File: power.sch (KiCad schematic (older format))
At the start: 52 parts, among them J2 USB_C_Receptacle_USB2.0, Q1 FS8205A, Q6 2N7002, Q7 AO3401A, Q8 2N7002, U3 SY7088, U4 XC6206P332MR, U5 DW01+G, U6 TP4056, U9 BQ34Z100

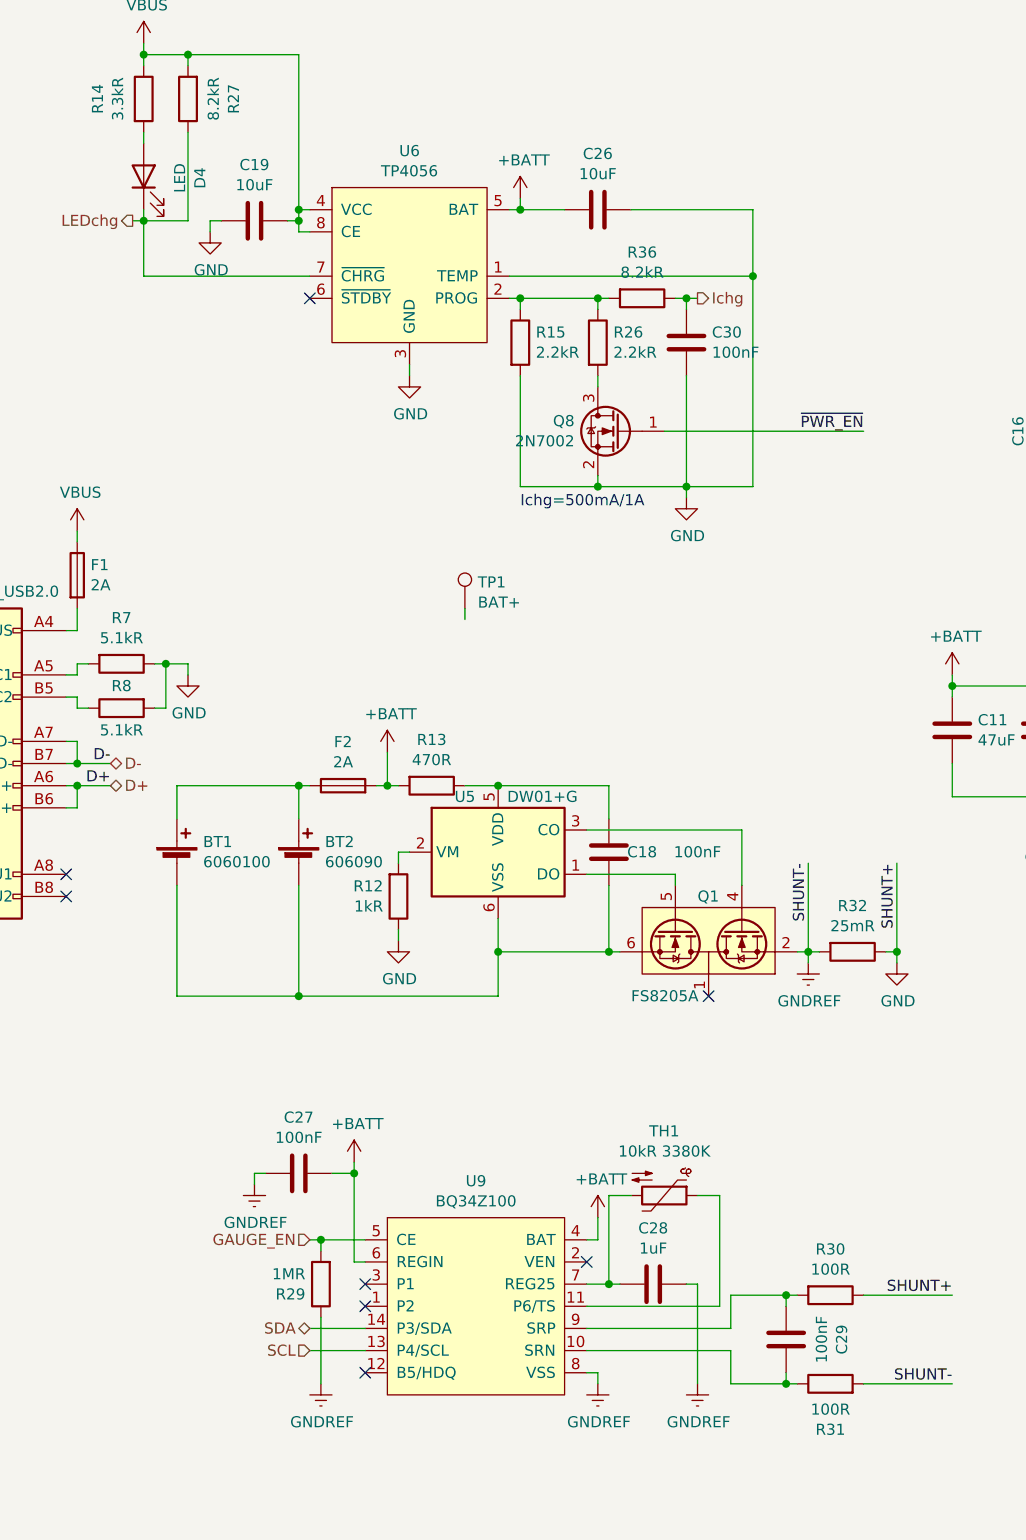
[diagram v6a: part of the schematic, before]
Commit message: Route SD interface
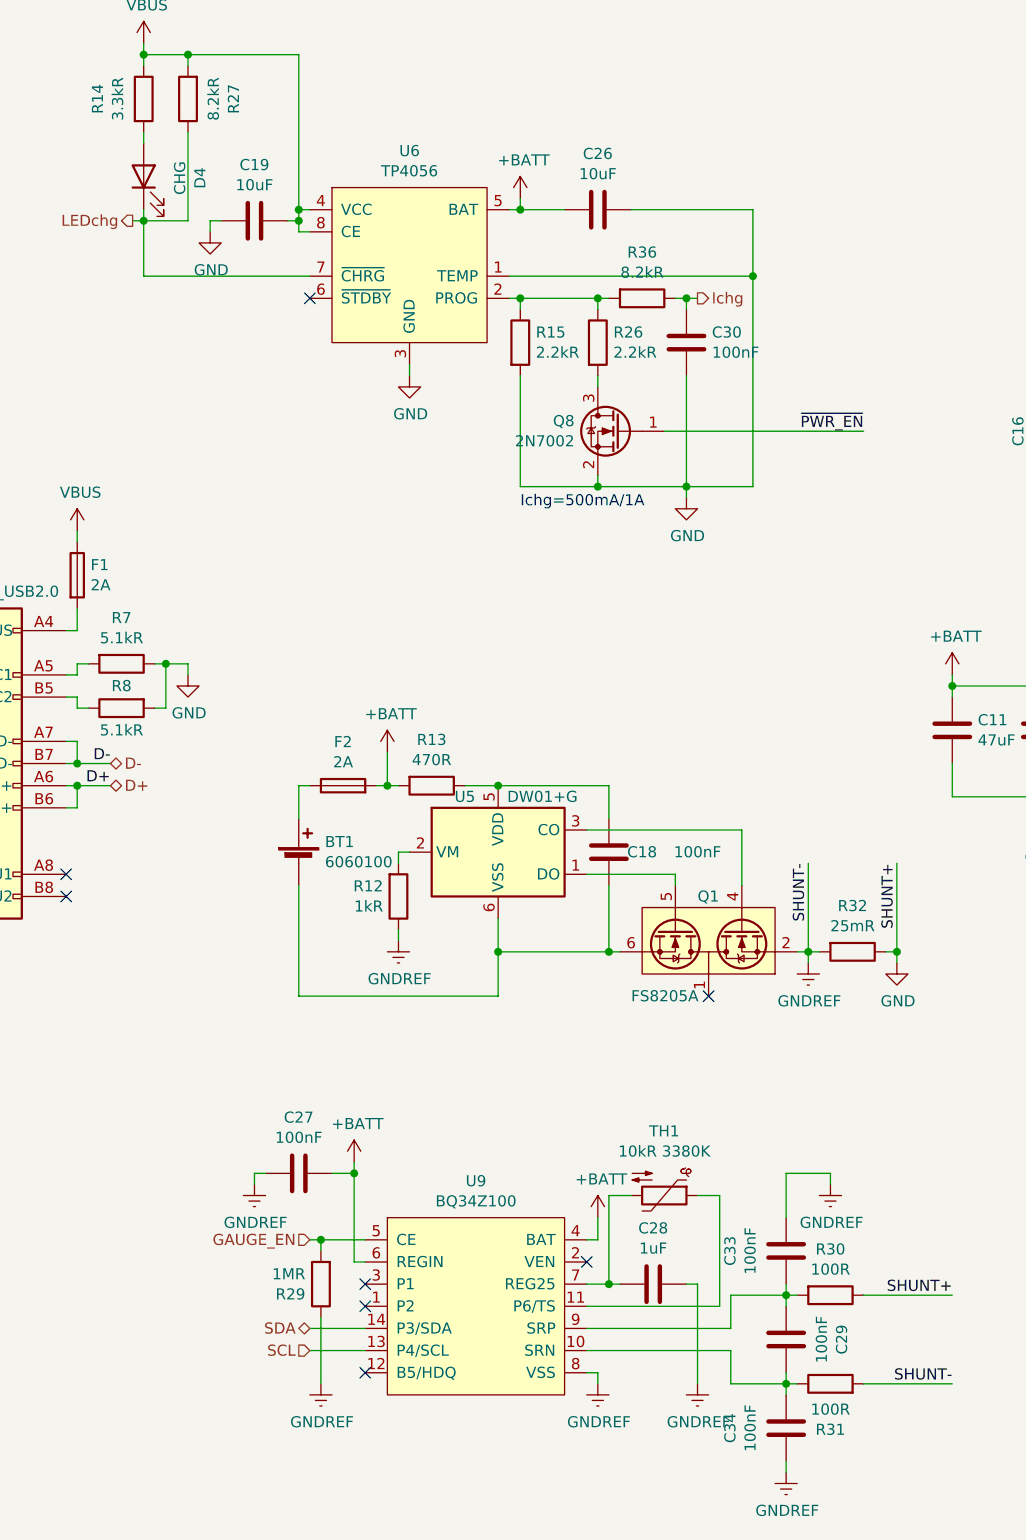
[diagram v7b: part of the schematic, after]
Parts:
- removed BT2: 606090, Battery_LiPo:LiPo_606090, symbol Device:Battery_Cell
- removed TP1: BAT+, TestPoint:TestPoint_Pad_4.0x4.0mm, symbol Connector:TestPoint
- added C33, C34: 100nF, Capacitor_SMD:C_0402_1005Metric, symbol Device:C
- D4: value LED -> CHG
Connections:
- net GND: no longer R12.1
- net GNDREF: now also R12.1, C33.2, C34.1
- net at C29.2, R31.1, U9.10 (SRN): now also C34.2
- net at C29.1, R30.2, U9.9 (SRP): now also C33.1
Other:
- moved on the sheet: BT1
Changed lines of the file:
@@
 	1    0    0    1
 $EndComp
-$Comp
-L power:GND #PWR?
-U 1 1 6057E172
-P 3150 4800
-AR Path="/6057E172" Ref="#PWR?"  Part="1"
-AR Path="/6051E9DC/6057E172" Ref="#PWR035"  Part="1"
-F 0 "#PWR035" H 3150 4550 50  0001 C CNN
-F 1 "GND" H 3155 4627 50  0000 C CNN
-F 2 "" H 3150 4800 50  0001 C CNN
-F 3 "" H 3150 4800 50  0001 C CNN
-	1    3150 4800
-	1    0    0    -1
-$EndComp
 Connection ~ 3600 4100
-$Comp
-L Connector:TestPoint TP?
-U 1 1 6057E186
-P 3450 3300
-AR Path="/6057E186" Ref="TP?"  Part="1"
-AR Path="/6051E9DC/6057E186" Ref="TP1"  Part="1"
-F 0 "TP1" H 3508 3418 50  0000 L CNN
-F 1 "BAT+" H 3508 3327 50  0000 L CNN
-F 2 "TestPoint:TestPoint_Pad_4.0x4.0mm" H 3650 3300 50  0001 C CNN
-F 3 "~" H 3650 3300 50  0001 C CNN
-	1    3450 3300
-	1    0    0    -1
-$EndComp
 $Comp
 L Transistor_FET_Dual:FS8205A Q?
@@
 AR Path="/6051E9DC/6057E1D2" Ref="D4"  Part="1"
 F 0 "D4" H 1993 1095 50  0000 C CNN
-F 1 "LED" H 1993 1186 50  0000 C CNN
+F 1 "CHG" H 1993 1186 50  0000 C CNN
 F 2 "LED_SMD:LED_0603_1608Metric" H 2000 1350 50  0001 C CNN
 F 3 "" H 2000 1350 50  0001 C CNN
@@
 	0    -1   -1   0
 $EndComp
-Wire Wire Line
-	3450 3350 3450 3300
 $Comp
 L Device:R R?
@@
 	3150 4450 3150 4400
 $Comp
-L Device:Battery_Cell BT2
-U 1 1 61944CD6
+L Device:Battery_Cell BT1
+U 1 1 6195E7B9
 P 2700 4450
-F 0 "BT2" H 2818 4546 50  0000 L CNN
-F 1 "606090" H 2818 4455 50  0000 L CNN
-F 2 "Battery_LiPo:LiPo_606090" V 2700 4510 50  0001 C CNN
+F 0 "BT1" H 2818 4546 50  0000 L CNN
+F 1 "6060100" H 2818 4455 50  0000 L CNN
+F 2 "Battery_LiPo:LiPo_6060100" V 2700 4510 50  0001 C CNN
 F 3 "~" V 2700 4510 50  0001 C CNN
 	1    2700 4450
 	1    0    0    -1
 $EndComp
-$Comp
-L Device:Battery_Cell BT1
-U 1 1 6195E7B9
-P 2150 4450
-F 0 "BT1" H 2268 4546 50  0000 L CNN
-F 1 "6060100" H 2268 4455 50  0000 L CNN
-F 2 "Battery_LiPo:LiPo_6060100" V 2150 4510 50  0001 C CNN
-F 3 "~" V 2150 4510 50  0001 C CNN
-	1    2150 4450
-	1    0    0    -1
-$EndComp
 Wire Wire Line
 	3050 4100 3100 4100
@@
 Connection ~ 3600 4850
 Wire Wire Line
-	2700 5050 2150 5050
-Wire Wire Line
-	2150 5050 2150 4550
-Connection ~ 2700 5050
-Wire Wire Line
-	2150 4100 2150 4250
-Wire Wire Line
 	2700 4250 2700 4100
 Wire Wire Line
-	2150 4100 2700 4100
-Connection ~ 2700 4100
-Wire Wire Line
 	2700 4100 2750 4100
+$Comp
+L Device:C C?
+U 1 1 61A24F0F
+P 4900 6200
+AR Path="/61A24F0F" Ref="C?"  Part="1"
+AR Path="/6051E9DC/61A24F0F" Ref="C33"  Part="1"
+F 0 "C33" V 5152 6200 50  0000 C CNN
+F 1 "100nF" V 5061 6200 50  0000 C CNN
+F 2 "Capacitor_SMD:C_0402_1005Metric" H 4938 6050 50  0001 C CNN
+F 3 "~" H 4900 6200 50  0001 C CNN
+F 4 "C1525" H 4900 6200 50  0001 C CNN "LCSC"
+	1    4900 6200
+	-1   0    0    1
+$EndComp
+$Comp
+L Device:C C?
+U 1 1 61A31217
+P 4900 7000
+AR Path="/61A31217" Ref="C?"  Part="1"
+AR Path="/6051E9DC/61A31217" Ref="C34"  Part="1"
+F 0 "C34" V 5152 7000 50  0000 C CNN
+F 1 "100nF" V 5061 7000 50  0000 C CNN
+F 2 "Capacitor_SMD:C_0402_1005Metric" H 4938 6850 50  0001 C CNN
+F 3 "~" H 4900 7000 50  0001 C CNN
+F 4 "C1525" H 4900 7000 50  0001 C CNN "LCSC"
+	1    4900 7000
+	-1   0    0    1
+$EndComp
+$Comp
+L power:GNDREF #PWR0130
+U 1 1 61A3D59D
+P 4900 7200
+F 0 "#PWR0130" H 4900 6950 50  0001 C CNN
+F 1 "GNDREF" H 4905 7027 50  0000 C CNN
+F 2 "" H 4900 7200 50  0001 C CNN
+F 3 "" H 4900 7200 50  0001 C CNN
+	1    4900 7200
+	1    0    0    -1
+$EndComp
+Wire Wire Line
+	4900 7200 4900 7150
+Wire Wire Line
+	4900 6850 4900 6800
+$Comp
+L power:GNDREF #PWR0131
+U 1 1 61A62F88
+P 5100 5900
+F 0 "#PWR0131" H 5100 5650 50  0001 C CNN
+F 1 "GNDREF" H 5105 5727 50  0000 C CNN
+F 2 "" H 5100 5900 50  0001 C CNN
+F 3 "" H 5100 5900 50  0001 C CNN
+	1    5100 5900
+	1    0    0    -1
+$EndComp
+Wire Wire Line
+	5100 5900 5100 5850
+Wire Wire Line
+	5100 5850 4900 5850
+Wire Wire Line
+	4900 5850 4900 6050
+Wire Wire Line
+	4900 6350 4900 6400
+$Comp
+L power:GNDREF #PWR0132
+U 1 1 61B1F64A
+P 3150 4800
+F 0 "#PWR0132" H 3150 4550 50  0001 C CNN
+F 1 "GNDREF" H 3155 4627 50  0000 C CNN
+F 2 "" H 3150 4800 50  0001 C CNN
+F 3 "" H 3150 4800 50  0001 C CNN
+	1    3150 4800
+	1    0    0    -1
+$EndComp
 $EndSCHEMATC
